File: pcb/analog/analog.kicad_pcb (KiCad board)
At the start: 2 copper layers, 70 x 70 mm, 72 parts, among them J1 USB_C_Receptacle_USB2.0, SW1 SW_Push, SW2 SW_Push, U1 SRV05-4, U10 RP2040, U11 W25Q128JVS, U2 XC6206P332MR, U3 DRV5056A3xDBZxQ1, U4 DRV5056A3xDBZxQ1, U5 DRV5056A3xDBZxQ1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

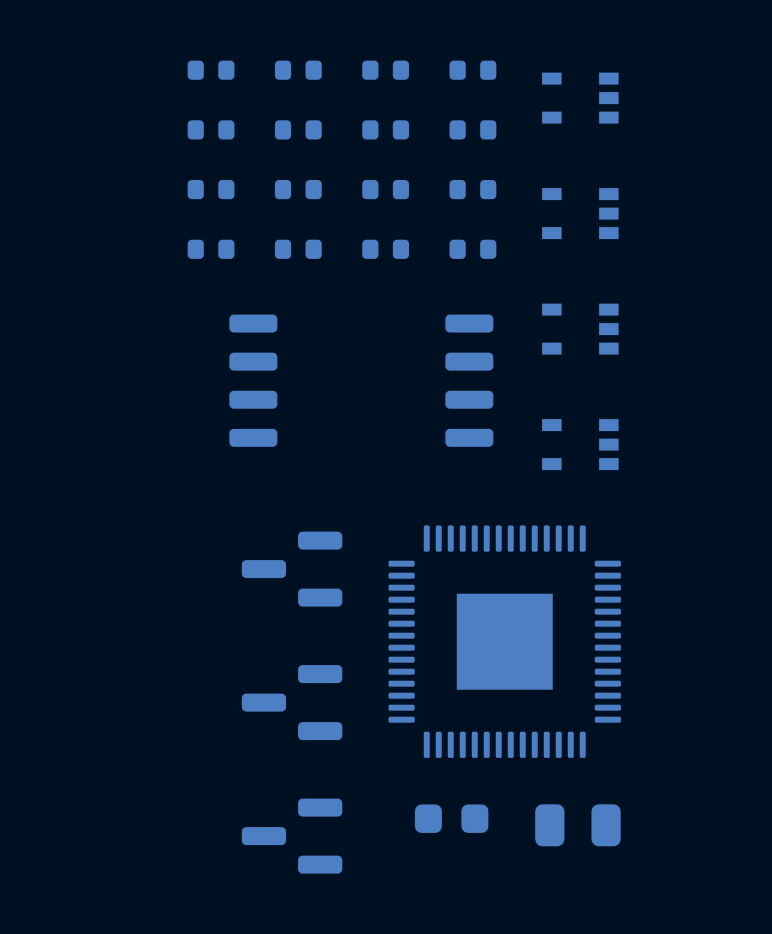
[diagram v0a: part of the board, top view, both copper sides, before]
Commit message: refactor: drive switch LEDs from a single output pin
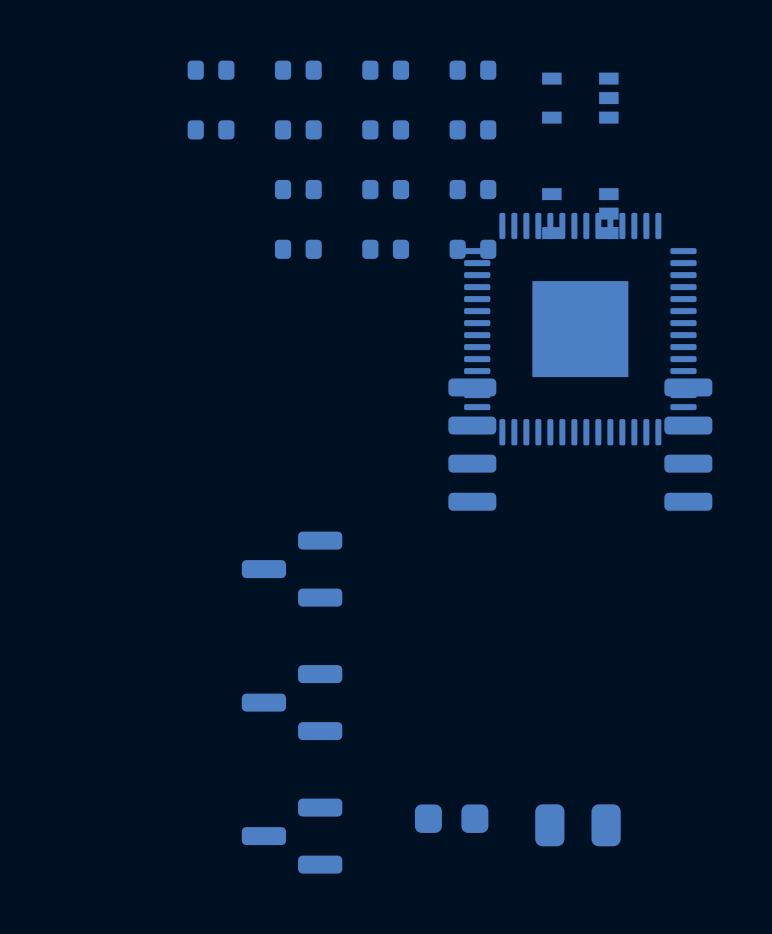
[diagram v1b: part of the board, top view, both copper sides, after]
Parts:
- removed R15: 5k1, Resistor_SMD:R_0402_1005Metric
- removed R16: 1k, Resistor_SMD:R_0402_1005Metric
- removed U10: RP2040, Package_DFN_QFN:QFN-56-1EP_7x7mm_P0.4mm_EP3.2x3.2mm
- removed U11: W25Q128JVS, Package_SO:SOIC-8_5.23x5.23mm_P1.27mm
- R10: value 1k -> 5k1
- R13: value 27 -> 5k1
- R14: value 5k1 -> 1k
- R9: value 1k -> 27
- U8: value 74AHCT1G125 -> RP2040; footprint Package_TO_SOT_SMD:SOT-353_SC-70-5 -> Package_DFN_QFN:QFN-56-1EP_7x7mm_P0.4mm_EP3.2x3.2mm
- U9: value 74AHCT1G125 -> W25Q128JVS; footprint Package_TO_SOT_SMD:SOT-353_SC-70-5 -> Package_SO:SOIC-8_5.23x5.23mm_P1.27mm
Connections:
- LED1 pad 2: unconnected-(LED1-DOUT-Pad2) -> Net-(LED1-DOUT)
- LED2 pad 2: unconnected-(LED2-DOUT-Pad2) -> Net-(LED2-DOUT)
- LED2 pad 3: Net-(LED2-DIN) -> Net-(LED1-DOUT)
- LED3 pad 3: Net-(LED3-DIN) -> Net-(LED2-DOUT)
- R10 pad 1: Net-(R10-Pad1) -> +3V3
- R10 pad 2: GND -> Net-(R10-Pad2)
- R11 pad 1: D+ -> D-
- R11 pad 2: Net-(U10-USB_DP) -> Net-(U8-USB_DM)
- R12 pad 2: Net-(R12-Pad2) -> RESET
- R13 pad 1: D- -> Net-(R10-Pad2)
- R13 pad 2: Net-(U10-USB_DM) -> Q_SEL
- R14 pad 1: +3V3 -> Net-(R14-Pad1)
- R14 pad 2: RESET -> Q_SEL
- R7 pad 1: Net-(R7-Pad1) -> Net-(C25-Pad2)
- R7 pad 2: GND -> XOUT
- R9 pad 1: Net-(C25-Pad2) -> D+
- R9 pad 2: XOUT -> Net-(U8-USB_DP)
- SW2 pad 2: Net-(R16-Pad1) -> Net-(R14-Pad1)
- U6 pad 2: RGB_HS0 -> RGB_HS
- U7 pad 1: Net-(R7-Pad1) -> Net-(R8-Pad1)
- U7 pad 2: RGB_HS1 -> RGB_GLOW
- U7 pad 4: Net-(LED2-DIN) -> Net-(D1-DIN)
- U8 pad 1: Net-(R8-Pad1) -> +3V3
- U8 pad 2: RGB_HS2 -> unconnected-(U8-GPIO0-Pad2)
- U8 pad 3: GND -> unconnected-(U8-GPIO1-Pad3)
- U8 pad 4: Net-(LED3-DIN) -> unconnected-(U8-GPIO2-Pad4)
- U8 pad 5: +5V -> unconnected-(U8-GPIO3-Pad5)
- U9 pad 1: Net-(R10-Pad1) -> Q_SEL
- U9 pad 2: RGB_GLOW -> Q_IO1
- U9 pad 3: GND -> Q_IO2
- U9 pad 4: Net-(D1-DIN) -> GND
- U9 pad 5: +5V -> Q_IO0

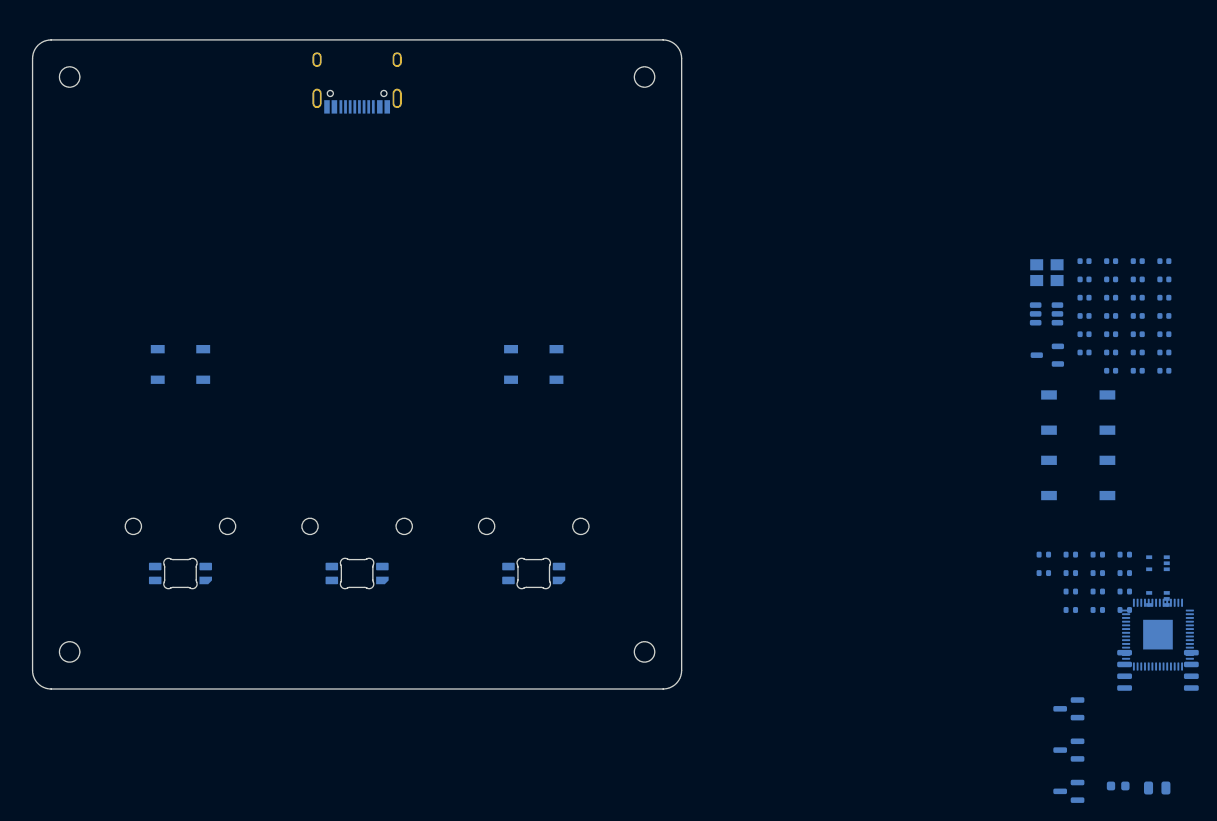
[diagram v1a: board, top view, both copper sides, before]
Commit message: feat: routing for new pcb required shuffling some components around, but this casn be accounted for in software, so it's not a big deal.
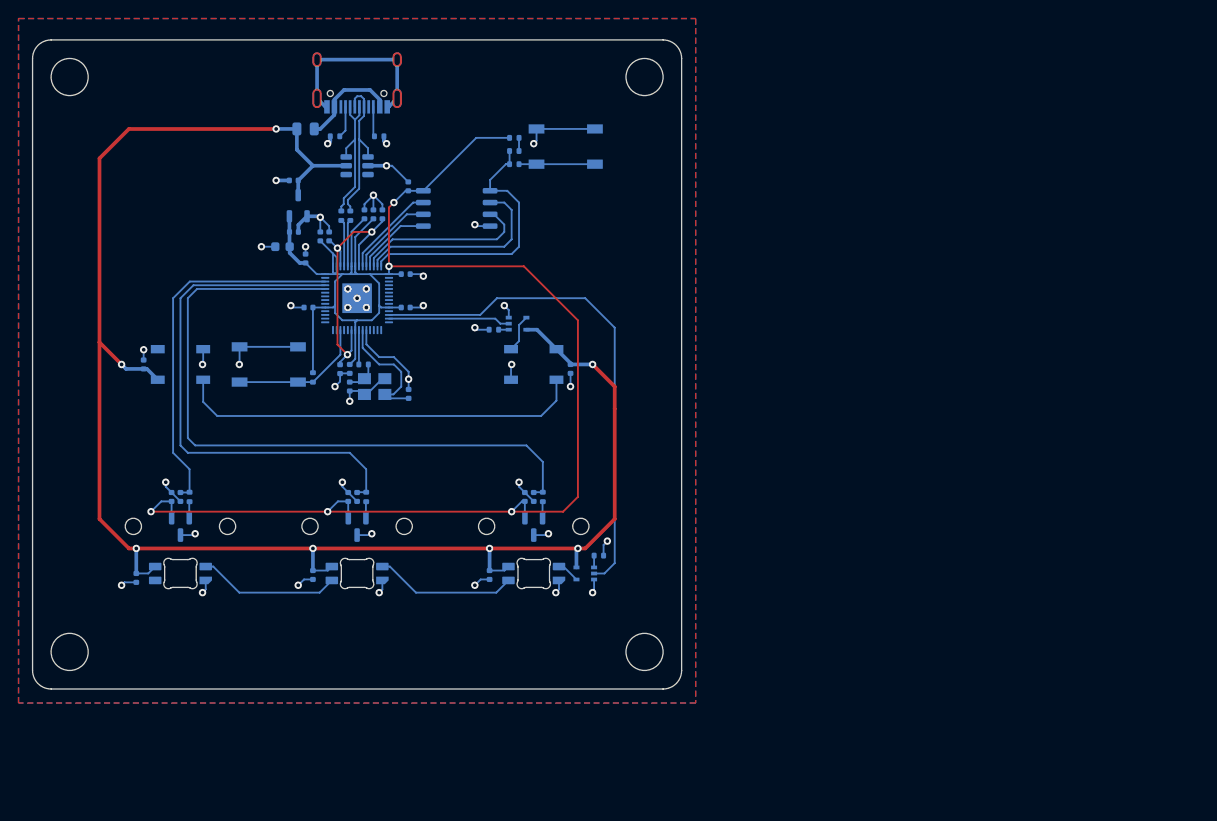
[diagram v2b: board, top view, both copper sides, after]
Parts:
- H4, H5, H6, H7: value M2 Screw -> 4mm Mounting Hole; footprint MountingHole:MountingHole_2.2mm_M2 -> MountingHole:MountingHole_4mm
- J1: footprint Connector_USB:USB_C_Receptacle_HRO_TYPE-C-31-M-12 -> PCM_marbastlib-various:USB_C_Receptacle_HRO_TYPE-C-31-M-12
- moved F1 116.1 mm to (45.2, 25.4), turned to 0 degrees
- moved C11 111.6 mm to (27.0, 73.8), turned to 90 degrees
- moved C3 109.2 mm to (30.8, 65.1), turned to 90 degrees
- moved C15 107.3 mm to (42.8, 38.1)
- moved C8 106.3 mm to (31.8, 65.1), turned to 90 degrees
- moved C26 101.6 mm to (27.8, 50.8), turned to -90 degrees
- moved U5 100.0 mm to (31.8, 68.3), turned to -90 degrees
- moved R5 98.1 mm to (32.7, 65.1), turned to 90 degrees
- moved R1 96.4 mm to (48.4, 26.2)
- moved C4 95.0 mm to (44.0, 31.0)
- moved C5 94.5 mm to (44.0, 36.5), turned to 0 degrees
- moved C10 93.8 mm to (46.0, 73.5), turned to 90 degrees
- moved U8 93.7 mm to (50.8, 43.7)
- moved R2 93.2 mm to (53.2, 26.2), turned to 0 degrees
- moved C2 91.1 mm to (49.8, 65.1), turned to 90 degrees
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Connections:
- U8 pad 12: unconnected-(U8-GPIO9-Pad12) -> RGB_HS
- U8 pad 13: unconnected-(U8-GPIO10-Pad13) -> RGB_GLOW
- U8 pad 14: RGB_HS0 -> unconnected-(U8-GPIO11-Pad14)
- U8 pad 36: RGB_GLOW -> unconnected-(U8-GPIO24-Pad36)
- U8 pad 38: HS2 -> HS0
- U8 pad 40: HS0 -> HS2
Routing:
- net +3V3: track 0.00 -> 193.1 mm, vias 0 -> 5
- net +5V: track 0.00 -> 182.5 mm, vias 0 -> 7
- net GND: track 0.00 -> 118.4 mm, vias 0 -> 42
- net HS0: track 0.00 -> 73.9 mm
- net HS1: track 0.00 -> 56.6 mm
- net RGB_HS: track 0.00 -> 54.5 mm
- net Net-(D1-DOUT): track 0.00 -> 44.1 mm
- net HS2: track 0.00 -> 39.8 mm
- net +1V1: track 0.00 -> 30.1 mm, vias 0 -> 3
- net Q_SEL: track 0.00 -> 29.9 mm
- net Q_IO1: track 0.00 -> 21.9 mm
- net Q_IO2: track 0.00 -> 18.9 mm
- net D+: track 0.00 -> 17.3 mm
- net D-: track 0.00 -> 15.9 mm
- net Net-(LED1-DOUT): track 0.00 -> 15.3 mm
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- added copper zone on B.Cu, net GND
- added copper zone on F.Cu, net GND

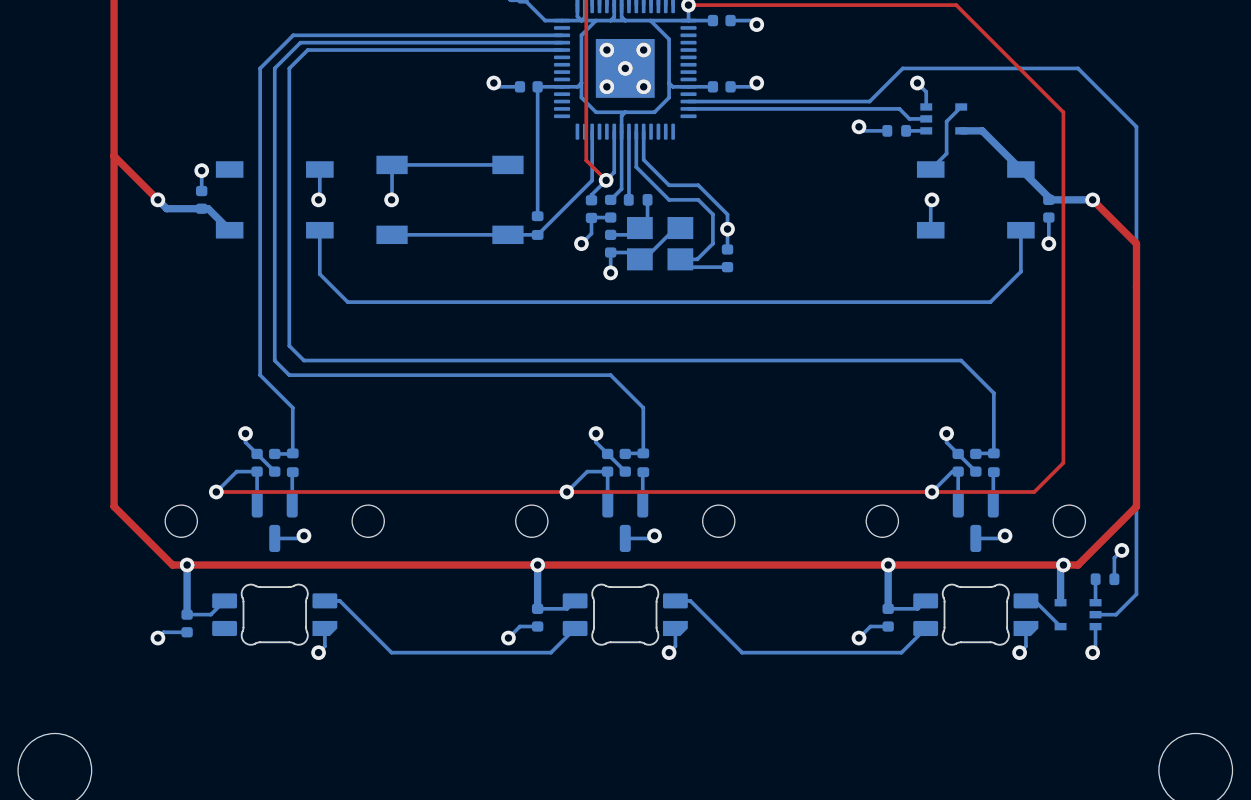
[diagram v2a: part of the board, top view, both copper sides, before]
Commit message: refactor: re-route power and signals for switch LEDs
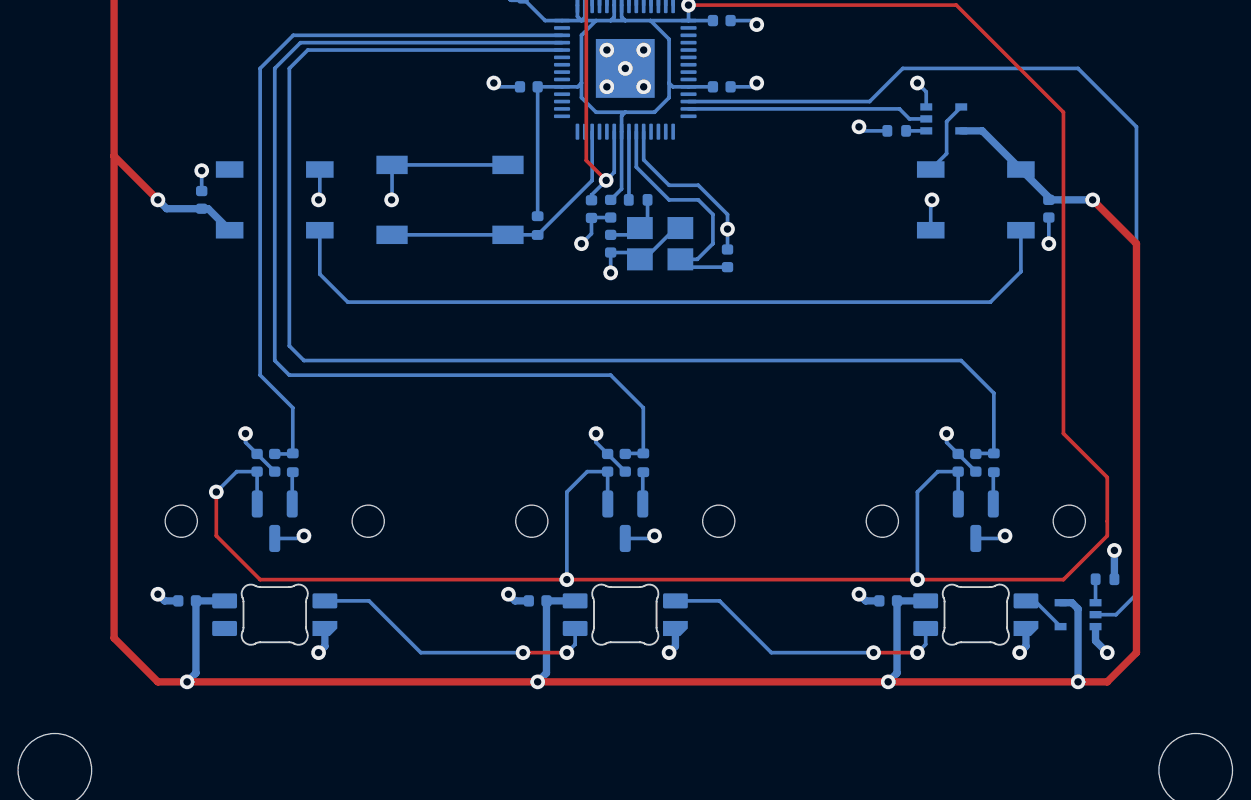
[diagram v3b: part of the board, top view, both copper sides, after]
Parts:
- moved C11 1.23 mm to (27.0, 72.6), turned to 0 degrees
- moved C10 0.91 mm to (46.0, 72.6), turned to 0 degrees
- moved C9 0.91 mm to (65.1, 72.6), turned to 0 degrees
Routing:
- net +3V3: track 193.1 -> 214.4 mm
- net +5V: track 182.5 -> 203.8 mm
- net GND: track 118.4 -> 116.8 mm
- net Net-(LED2-DOUT): track 15.3 -> 15.8 mm, vias 0 -> 2
- net Net-(LED1-DOUT): track 15.3 -> 15.8 mm, vias 0 -> 2

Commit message: feat: add haruka emote on back of pcb
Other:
- board text added: "Harukapad rev. 1 Designed by Ace4896"
